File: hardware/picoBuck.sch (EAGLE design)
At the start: 37 parts, among them U1 AL8805, U2 AL8805, U3 AL8805

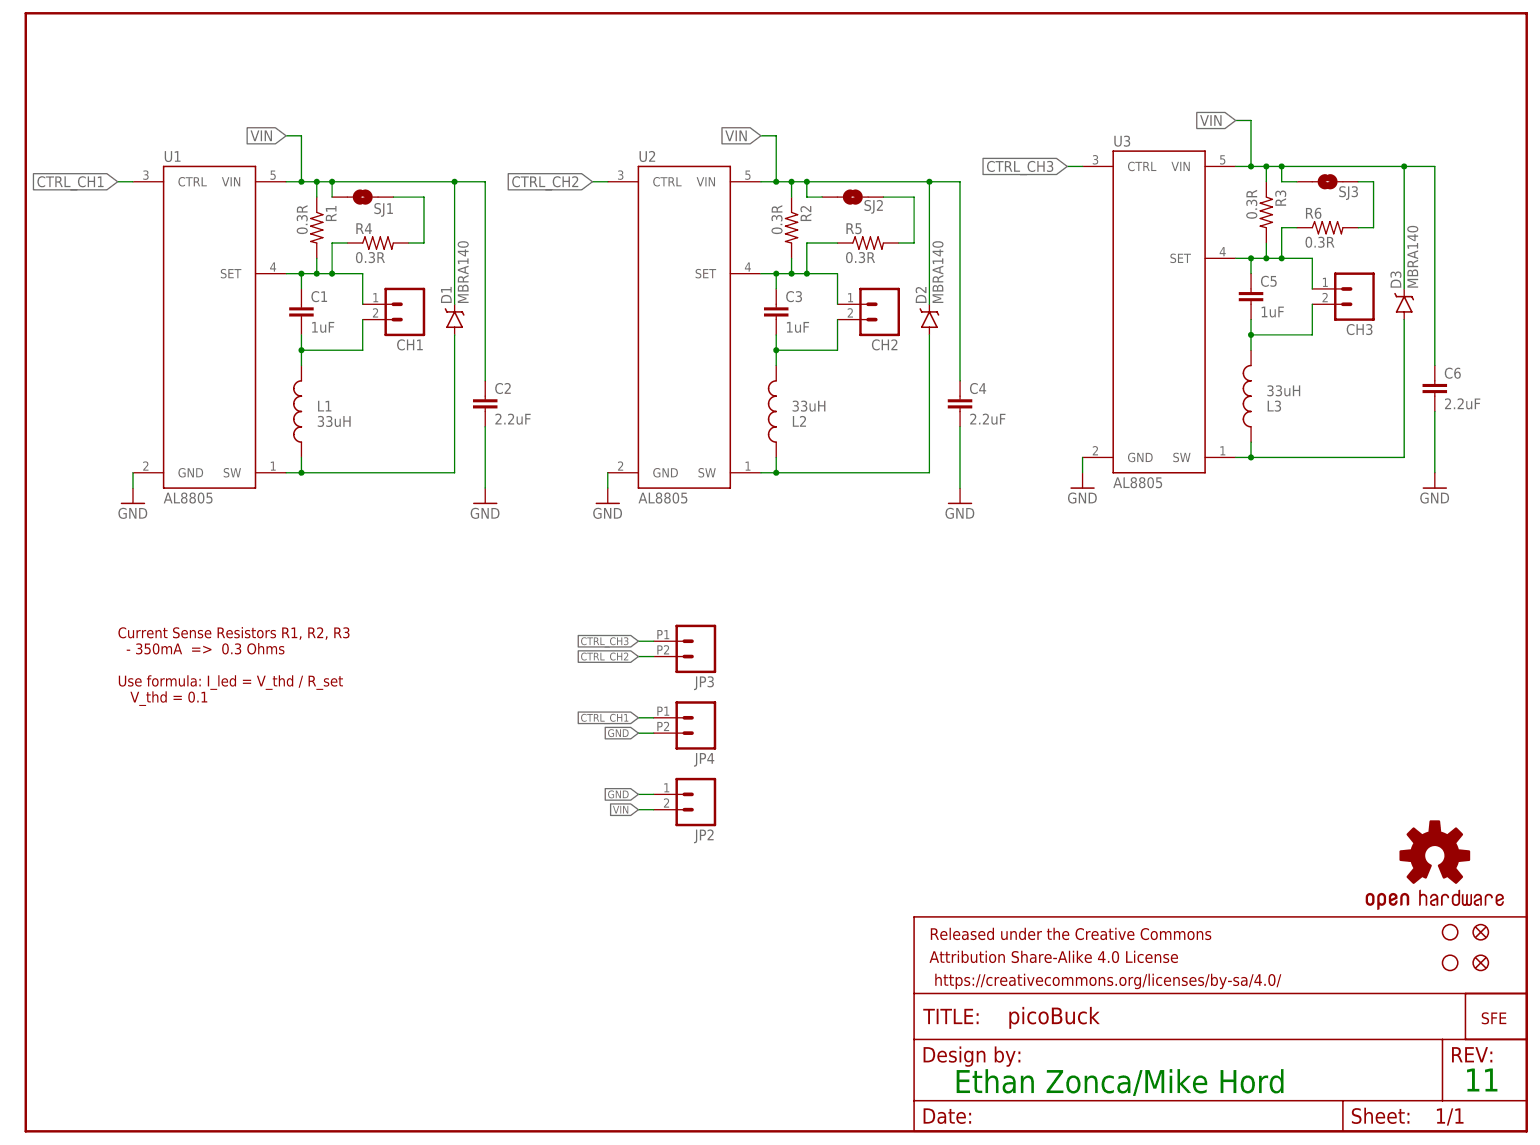
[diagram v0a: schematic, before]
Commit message: AL8805 buck LED driver EOL, replace with AL8860
* Replaced AL8805 with AL8860 drop in replacement
* Bumped version number on board and schematic
* Created schematic pdf and zip folder of eagle files for the product page
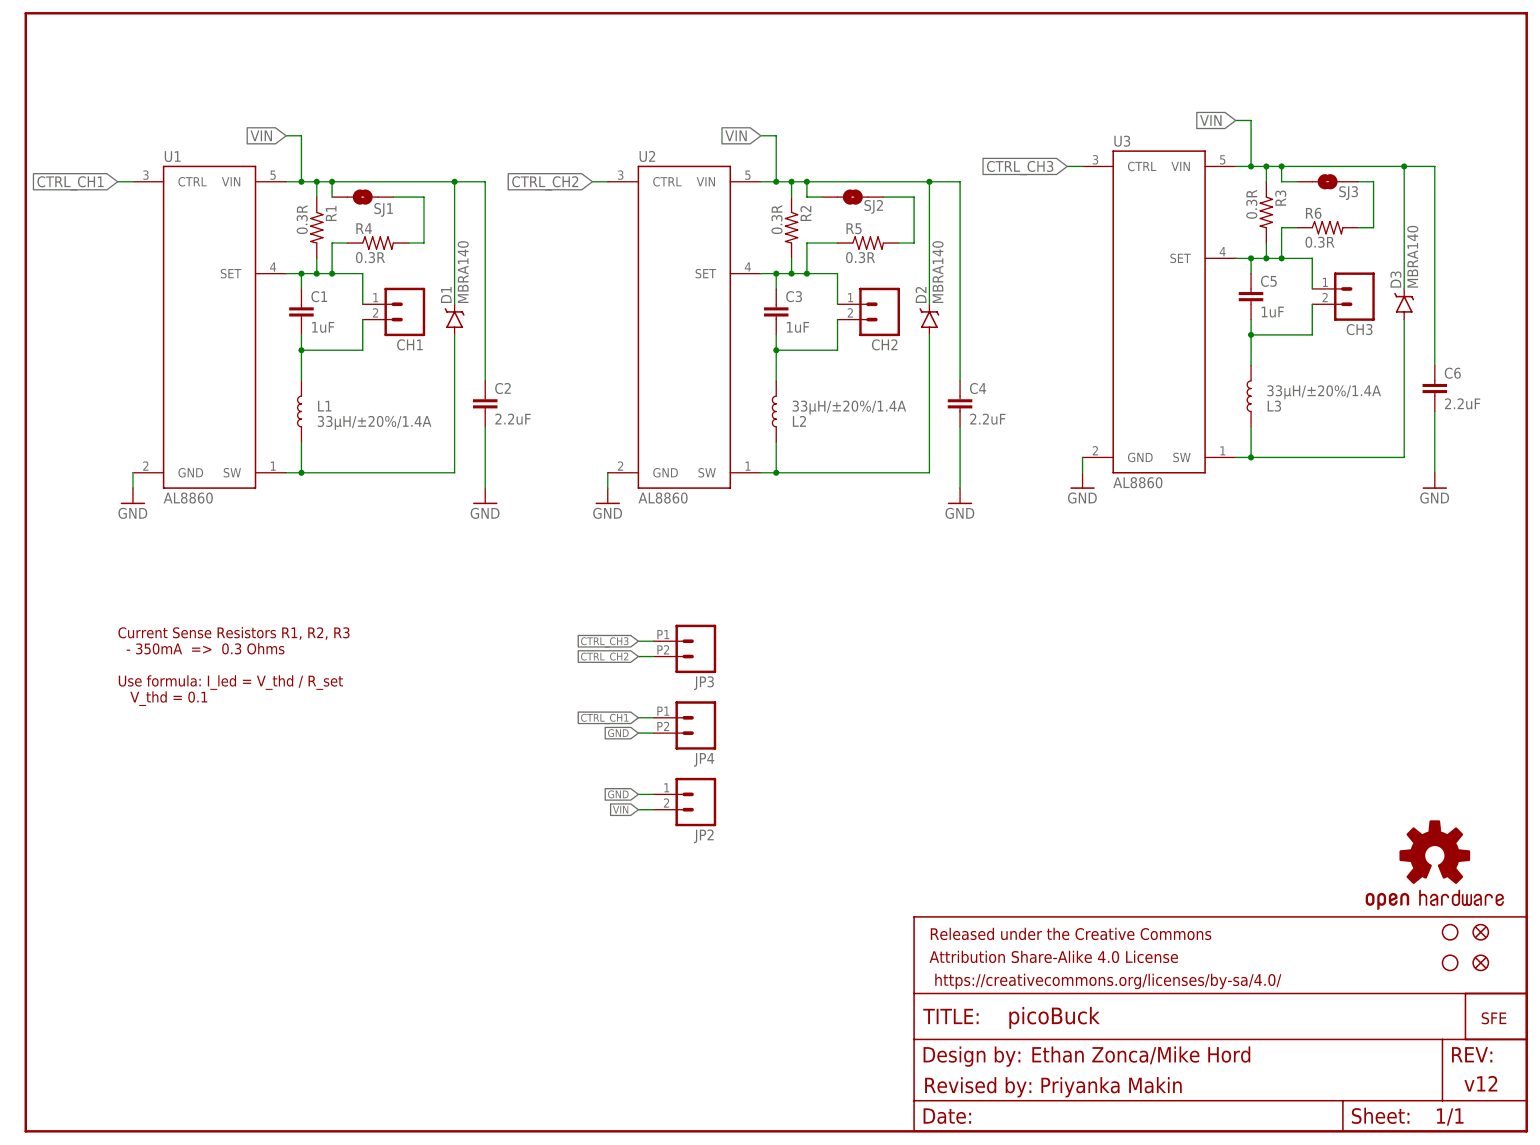
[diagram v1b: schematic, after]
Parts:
- CH1, CH2, CH3, JP2: device SparkFun:M023.5MM_LOCK -> SparkFun-Connectors:CONN_023.5MM_LOCK
- L1, L2, L3: value 33uH -> 33µH/±20%/1.4A; device SparkFun-Passives:INDUCTORBOURNS_SRN6045 -> SparkFun-Coils:INDUCTOR-SRN6045-33UH
- SJ1, SJ2, SJ3: value JUMPER-PAD-2-NO -> JUMPER-SMT_2_NO_NO-SILK; device SparkFun-Passives:JUMPER-PAD-2-NO -> SparkFun-Jumpers:JUMPER-SMT_2_NO_NO-SILK
- U1, U2, U3: value AL8805 -> AL8860; device SparkFun-PowerIC:AL8805 -> SparkFun-IC-Special-Function:AL8860SOT23
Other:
- note added: "Revised by: Priyanka Makin"
- note added: "v12"
- note removed: "11"
